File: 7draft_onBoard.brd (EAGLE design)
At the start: 89.8 x 88.9 mm, 81 parts, among them IC3 74ABT125PW, IC4 MAX4466KS, J2 USB_MINI-B_DIGIKEY, Q1 NPN 40V 1A SOT-23

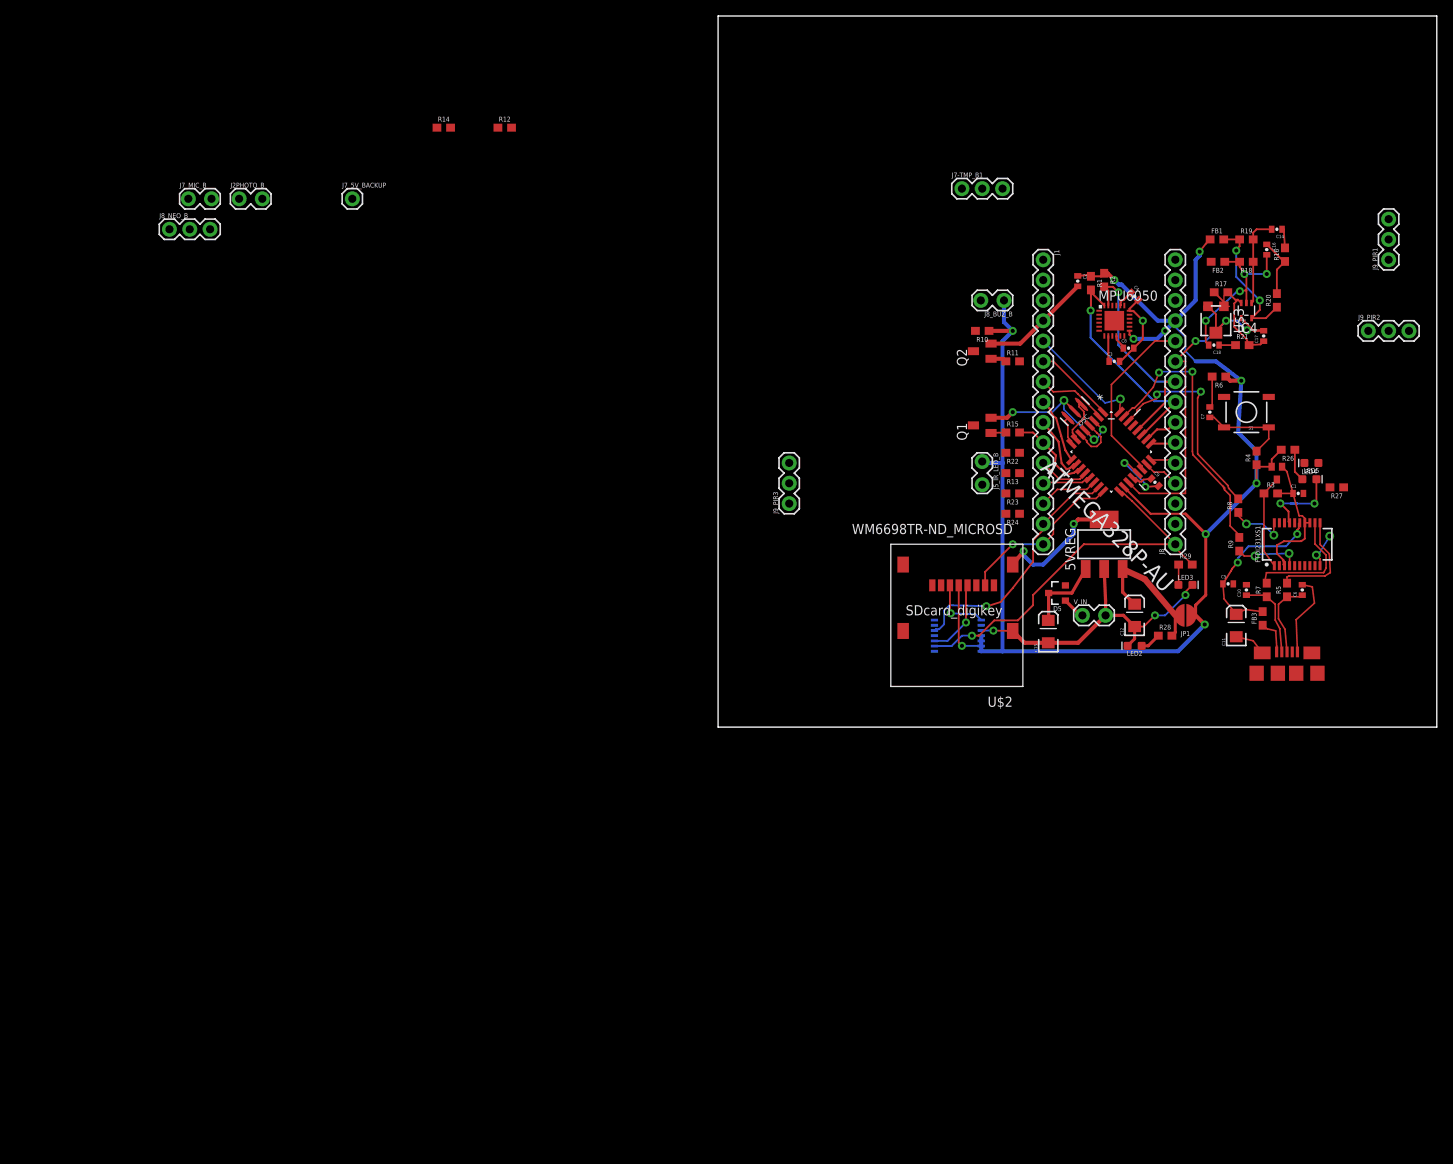
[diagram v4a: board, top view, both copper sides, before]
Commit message: everything is added. IR fixed, beam break fixed. neo pixel added for fun this will be addressed at 1 and the one at top is addressed at 2
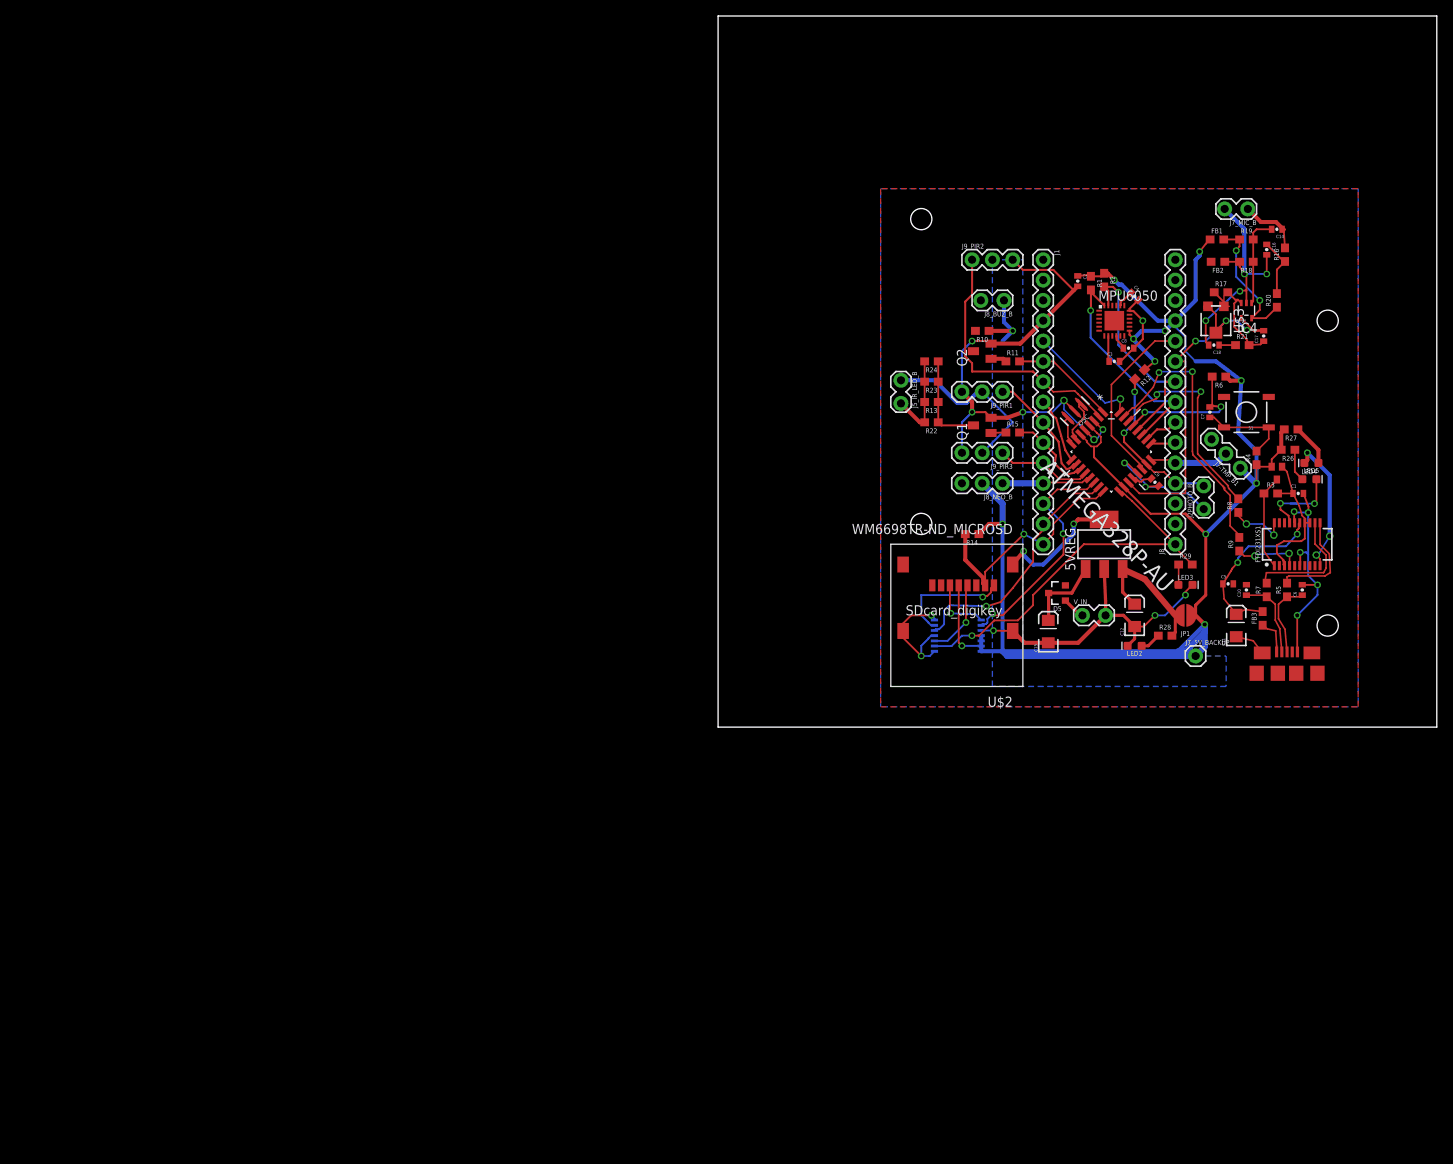
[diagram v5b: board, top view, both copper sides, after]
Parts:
- moved J7_MIC_B 132.1 mm to (66.0, 64.8), turned to 180 degrees
- moved J2PHOTO_B 126.4 mm to (60.7, 27.4), turned to 90 degrees
- moved J7_5V_BACKUP 119.9 mm to (59.7, 8.89)
- moved J8_NEO_B 108.9 mm to (35.6, 30.5), turned to 180 degrees
- moved R12 85.2 mm to (52.7, 44.1), turned to 225 degrees
- moved R14 83.3 mm to (31.8, 24.1), turned to 180 degrees
- moved J9_PIR1 51.0 mm to (35.6, 41.9), turned to 180 degrees
- moved J9_PIR2 50.3 mm to (31.8, 58.4)
- moved J7-TMP_B1 49.3 mm to (65.3, 32.4), turned to 135 degrees
- moved J9_PIR3 27.4 mm to (35.6, 34.3), turned to 180 degrees
- moved R24 21.6 mm to (26.7, 45.7)
- moved R23 17.3 mm to (26.7, 43.2)
- moved J5_IR_LED_B 14.4 mm to (22.9, 43.2)
- moved R13 13.5 mm to (26.7, 40.6)
- moved R22 10.9 mm to (26.7, 38.1)
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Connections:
- net 5REGOUT: no longer J7_5V_BACKUP.1
- net 5V: now also J7_5V_BACKUP.1
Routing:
- net GND: track 148.6 -> 230.0 mm, vias 16 -> 25
- net 5V: track 201.7 -> 261.8 mm, vias 10 -> 12
- net D4: track 8.91 -> 33.0 mm
- net SS: track 7.44 -> 29.4 mm, vias 0 -> 2
- net A0: track 4.58 -> 20.6 mm, vias 0 -> 2
- net DAT1: track 0.00 -> 14.9 mm, vias 0 -> 1
- net RESET: track 3.92 -> 17.9 mm, vias 0 -> 2
- net TXLED: track 4.53 -> 17.5 mm, vias 2 -> 3
- net N$2: track 0.00 -> 12.2 mm
- net N$1: track 0.00 -> 11.6 mm
- net MISO: track 21.3 -> 29.6 mm
- net A1: track 3.18 -> 9.99 mm
- net D6: track 8.16 -> 14.8 mm
- net D8: track 6.40 -> 12.0 mm
- net MIC_IN_C14: track 2.53 -> 8.08 mm
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- added copper zone on layer 16, net 5V
- added copper zone on layer 1, net GND
- added copper zone on layer 16, net GND
